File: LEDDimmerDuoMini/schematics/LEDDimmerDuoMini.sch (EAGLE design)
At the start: 13 parts, among them IC1 7805T, T1 2N3904, T2 2N3904

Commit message: Update before LED flaate testen
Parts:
- added R3, R4: (no value), eagle-ltspice:R
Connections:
- new net N$7: Q2.G, R4.2, T2.E
- net PWM1: now also R3.1, R3.2
- net PWM2: now also R4.1; no longer Q2.G, T2.E
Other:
- moved on the sheet: Q2, R2, T2
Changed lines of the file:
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@@
 <layer number="97" name="Info" color="7" fill="1" visible="yes" active="yes"/>
 <layer number="98" name="Guide" color="6" fill="1" visible="yes" active="yes"/>
+<layer number="99" name="SpiceOrder" color="5" fill="1" visible="yes" active="yes"/>
 <layer number="100" name="Muster" color="7" fill="1" visible="no" active="no"/>
 <layer number="101" name="Patch_Top" color="12" fill="4" visible="yes" active="yes"/>
@@
 <part name="R2" library="rcl" deviceset="R-EU_" device="VTA52"/>
 <part name="GND4" library="SparkFun-Aesthetics" deviceset="GND" device=""/>
+<part name="R3" library="eagle-ltspice" deviceset="R" device=""/>
+<part name="R4" library="eagle-ltspice" deviceset="R" device=""/>
 </parts>
 <sheets>
@@
 <instance part="SUPPLY1" gate="G$1" x="101.6" y="22.86"/>
 <instance part="GND3" gate="1" x="91.44" y="-38.1"/>
-<instance part="Q2" gate="G$1" x="119.38" y="7.62"/>
-<instance part="T2" gate="G1" x="111.76" y="-7.62" rot="R180"/>
-<instance part="R2" gate="G$1" x="121.92" y="-22.86" rot="R90"/>
-<instance part="GND4" gate="1" x="121.92" y="-38.1"/>
+<instance part="Q2" gate="G$1" x="132.08" y="7.62"/>
+<instance part="T2" gate="G1" x="124.46" y="-7.62" rot="R180"/>
+<instance part="R2" gate="G$1" x="134.62" y="-22.86" rot="R90"/>
+<instance part="GND4" gate="1" x="134.62" y="-38.1"/>
+<instance part="R3" gate="G$1" x="73.66" y="5.08"/>
+<instance part="R4" gate="G$1" x="116.84" y="5.08"/>
 </instances>
 <busses>
@@
 <pinref part="R2" gate="G$1" pin="1"/>
 <pinref part="GND4" gate="1" pin="GND"/>
-<wire x1="121.92" y1="-27.94" x2="121.92" y2="-30.48" width="0.1524" layer="91"/>
+<wire x1="134.62" y1="-27.94" x2="134.62" y2="-30.48" width="0.1524" layer="91"/>
 <pinref part="T2" gate="G1" pin="C"/>
-<wire x1="121.92" y1="-30.48" x2="121.92" y2="-35.56" width="0.1524" layer="91"/>
-<wire x1="109.22" y1="-12.7" x2="109.22" y2="-30.48" width="0.1524" layer="91"/>
-<wire x1="109.22" y1="-30.48" x2="121.92" y2="-30.48" width="0.1524" layer="91"/>
-<junction x="121.92" y="-30.48"/>
+<wire x1="134.62" y1="-30.48" x2="134.62" y2="-35.56" width="0.1524" layer="91"/>
+<wire x1="121.92" y1="-12.7" x2="121.92" y2="-30.48" width="0.1524" layer="91"/>
+<wire x1="121.92" y1="-30.48" x2="134.62" y2="-30.48" width="0.1524" layer="91"/>
+<junction x="134.62" y="-30.48"/>
 </segment>
 </net>
@@
 <pinref part="T1" gate="G1" pin="E"/>
 <wire x1="78.74" y1="5.08" x2="78.74" y2="-2.54" width="0.1524" layer="91"/>
-<wire x1="78.74" y1="5.08" x2="71.12" y2="5.08" width="0.1524" layer="91"/>
+<pinref part="R3" gate="G$1" pin="2"/>
 <junction x="78.74" y="5.08"/>
-<label x="71.12" y="5.08" size="1.016" layer="95" rot="R180" xref="yes"/>
+</segment>
+<segment>
+<pinref part="R3" gate="G$1" pin="1"/>
+<wire x1="68.58" y1="5.08" x2="63.5" y2="5.08" width="0.1524" layer="91"/>
+<label x="63.5" y="5.08" size="1.016" layer="95" rot="R180" xref="yes"/>
 </segment>
 </net>
@@
 <wire x1="91.44" y1="20.32" x2="91.44" y2="12.7" width="0.1524" layer="91"/>
 <pinref part="Q2" gate="G$1" pin="D"/>
-<wire x1="121.92" y1="12.7" x2="121.92" y2="20.32" width="0.1524" layer="91"/>
+<wire x1="134.62" y1="12.7" x2="121.92" y2="20.32" width="0.1524" layer="91"/>
 </segment>
 </net>
@@
 </segment>
 <segment>
-<pinref part="Q2" gate="G$1" pin="G"/>
-<wire x1="116.84" y1="5.08" x2="109.22" y2="5.08" width="0.1524" layer="91"/>
-<pinref part="T2" gate="G1" pin="E"/>
-<wire x1="109.22" y1="5.08" x2="109.22" y2="-2.54" width="0.1524" layer="91"/>
-<wire x1="109.22" y1="5.08" x2="104.14" y2="5.08" width="0.1524" layer="91"/>
-<junction x="109.22" y="5.08"/>
-<label x="104.14" y="5.08" size="1.016" layer="95" rot="R180" xref="yes"/>
+<pinref part="R4" gate="G$1" pin="1"/>
+<wire x1="111.76" y1="5.08" x2="106.68" y2="5.08" width="0.1524" layer="91"/>
+<label x="106.68" y="5.08" size="1.016" layer="95" rot="R180" xref="yes"/>
 </segment>
 </net>
@@
 <segment>
 <pinref part="T2" gate="G1" pin="B"/>
-<wire x1="121.92" y1="-7.62" x2="114.3" y2="-7.62" width="0.1524" layer="91"/>
+<wire x1="134.62" y1="-7.62" x2="127" y2="-7.62" width="0.1524" layer="91"/>
 <pinref part="R2" gate="G$1" pin="2"/>
-<wire x1="121.92" y1="-7.62" x2="121.92" y2="-17.78" width="0.1524" layer="91"/>
+<wire x1="134.62" y1="-7.62" x2="134.62" y2="-17.78" width="0.1524" layer="91"/>
 <pinref part="Q2" gate="G$1" pin="S"/>
-<wire x1="121.92" y1="2.54" x2="121.92" y2="-7.62" width="0.1524" layer="91"/>
-<junction x="121.92" y="-7.62"/>
-</segment>
-</net>
+<wire x1="134.62" y1="2.54" x2="134.62" y2="-7.62" width="0.1524" layer="91"/>
+<junction x="134.62" y="-7.62"/>
+</segment>
+</net>
+<net name="N$7" class="0">
+<segment>
+<pinref part="Q2" gate="G$1" pin="G"/>
+<pinref part="R4" gate="G$1" pin="2"/>
+<wire x1="129.54" y1="5.08" x2="121.92" y2="5.08" width="0.1524" layer="91"/>
+<pinref part="T2" gate="G1" pin="E"/>
+<wire x1="121.92" y1="-2.54" x2="121.92" y2="5.08" width="0.1524" layer="91"/>
+<junction x="121.92" y="5.08"/>
+</segment>
+</net>

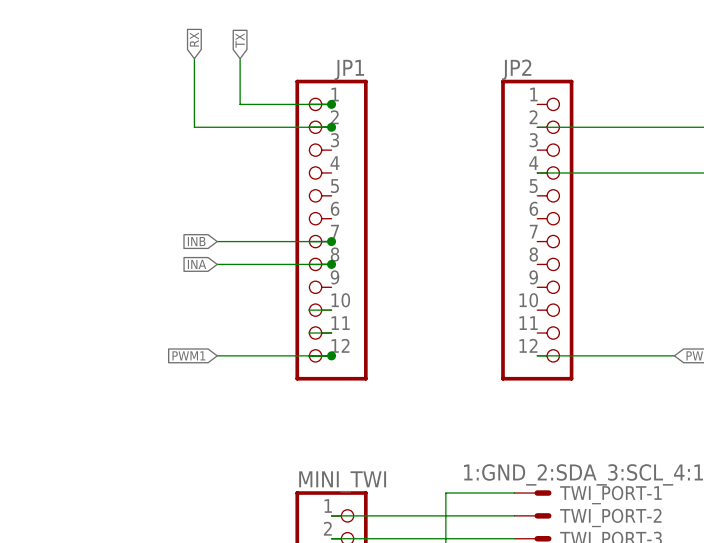
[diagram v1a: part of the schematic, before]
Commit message: Finished laying out components for LEEDDimmerDuoM<ini
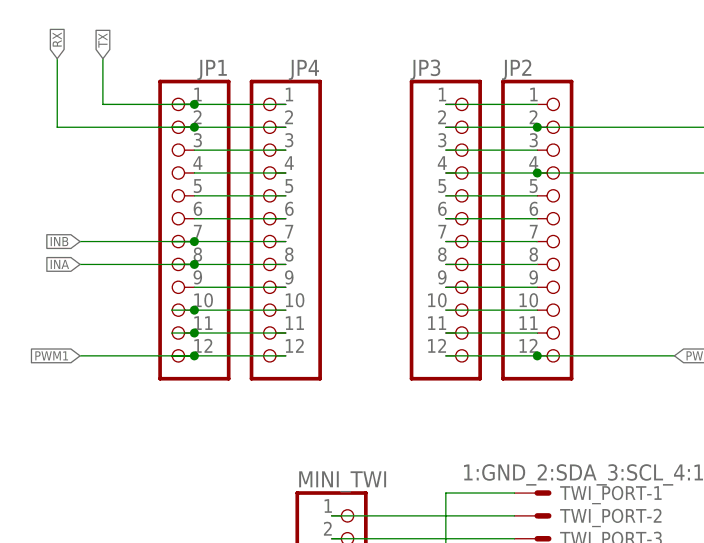
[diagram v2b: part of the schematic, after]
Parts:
- added JP3, JP4: (no value), pinhead:PINHD-1X12
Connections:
- new net N$12: JP1.6, JP4.6
- new net N$13: JP1.9, JP4.9
- new net N$15: JP2.1, JP3.1
- new net N$17: JP2.3, JP3.3
- new net N$19: JP2.5, JP3.5
- new net N$20: JP2.6, JP3.6
- new net N$21: JP2.7, JP3.7
- new net N$22: JP2.8, JP3.8
- new net N$23: JP2.9, JP3.9
- new net N$24: JP2.10, JP3.10
- new net N$25: JP2.11, JP3.11
- new net N$6: JP1.3, JP4.3
- new net N$8: JP1.4, JP4.4
- new net N$9: JP1.5, JP4.5
- net 5V: now also JP3.4
- net GND: now also JP3.2
- net INA: now also JP4.8
- net INB: now also JP4.7
- net N$10: now also JP4.11
- net N$11: now also JP4.10
- net PWM1: now also JP4.12
- net PWM2: now also JP3.12
- net RX: now also JP4.2
- net TX: now also JP4.1
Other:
- moved on the sheet: JP1
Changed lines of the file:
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@@
 <part name="R3" library="eagle-ltspice" deviceset="R" device=""/>
 <part name="R4" library="eagle-ltspice" deviceset="R" device=""/>
+<part name="JP3" library="pinhead" deviceset="PINHD-1X12" device=""/>
+<part name="JP4" library="pinhead" deviceset="PINHD-1X12" device=""/>
 </parts>
 <sheets>
@@
 <instance part="GND6" gate="1" x="121.92" y="124.46" rot="R90"/>
 <instance part="SUPPLY3" gate="G$1" x="127" y="119.38" rot="R270"/>
-<instance part="JP1" gate="G$1" x="73.66" y="114.3" rot="MR0"/>
+<instance part="JP1" gate="G$1" x="58.42" y="114.3" rot="MR0"/>
 <instance part="JP2" gate="G$1" x="101.6" y="114.3"/>
 <instance part="TWI_PORT" gate="-1" x="99.06" y="83.82" smashed="yes">
@@
 <instance part="R3" gate="G$1" x="73.66" y="5.08"/>
 <instance part="R4" gate="G$1" x="116.84" y="5.08"/>
+<instance part="JP3" gate="G$1" x="91.44" y="114.3"/>
+<instance part="JP4" gate="G$1" x="68.58" y="114.3" rot="MR0"/>
 </instances>
 <busses>
@@
 <pinref part="GND6" gate="1" pin="GND"/>
 <wire x1="99.06" y1="124.46" x2="119.38" y2="124.46" width="0.1524" layer="91"/>
+<pinref part="JP3" gate="G$1" pin="2"/>
+<wire x1="88.9" y1="124.46" x2="99.06" y2="124.46" width="0.1524" layer="91"/>
+<junction x="99.06" y="124.46"/>
 </segment>
 <segment>
@@
 <net name="INB" class="0">
 <segment>
-<wire x1="73.66" y1="111.76" x2="76.2" y2="111.76" width="0.1524" layer="91"/>
-<label x="63.5" y="111.76" size="1.016" layer="95" rot="MR0" xref="yes"/>
+<wire x1="58.42" y1="111.76" x2="60.96" y2="111.76" width="0.1524" layer="91"/>
+<label x="48.26" y="111.76" size="1.016" layer="95" rot="MR0" xref="yes"/>
 <pinref part="JP1" gate="G$1" pin="7"/>
-<wire x1="76.2" y1="111.76" x2="63.5" y2="111.76" width="0.1524" layer="91"/>
-<junction x="76.2" y="111.76"/>
+<wire x1="60.96" y1="111.76" x2="48.26" y2="111.76" width="0.1524" layer="91"/>
+<junction x="60.96" y="111.76"/>
+<pinref part="JP4" gate="G$1" pin="7"/>
+<wire x1="71.12" y1="111.76" x2="60.96" y2="111.76" width="0.1524" layer="91"/>
 </segment>
 </net>
 <net name="PWM1" class="0">
 <segment>
-<wire x1="73.66" y1="99.06" x2="76.2" y2="99.06" width="0.1524" layer="91"/>
-<label x="63.5" y="99.06" size="1.016" layer="95" rot="MR0" xref="yes"/>
+<wire x1="58.42" y1="99.06" x2="60.96" y2="99.06" width="0.1524" layer="91"/>
+<label x="48.26" y="99.06" size="1.016" layer="95" rot="MR0" xref="yes"/>
 <pinref part="JP1" gate="G$1" pin="12"/>
-<wire x1="76.2" y1="99.06" x2="63.5" y2="99.06" width="0.1524" layer="91"/>
-<junction x="76.2" y="99.06"/>
+<wire x1="60.96" y1="99.06" x2="48.26" y2="99.06" width="0.1524" layer="91"/>
+<junction x="60.96" y="99.06"/>
+<pinref part="JP4" gate="G$1" pin="12"/>
+<wire x1="71.12" y1="99.06" x2="60.96" y2="99.06" width="0.1524" layer="91"/>
 </segment>
 <segment>
@@
 <net name="INA" class="0">
 <segment>
-<wire x1="73.66" y1="109.22" x2="76.2" y2="109.22" width="0.1524" layer="91"/>
-<label x="63.5" y="109.22" size="1.016" layer="95" rot="MR0" xref="yes"/>
+<wire x1="58.42" y1="109.22" x2="60.96" y2="109.22" width="0.1524" layer="91"/>
+<label x="48.26" y="109.22" size="1.016" layer="95" rot="MR0" xref="yes"/>
 <pinref part="JP1" gate="G$1" pin="8"/>
-<wire x1="76.2" y1="109.22" x2="63.5" y2="109.22" width="0.1524" layer="91"/>
-<junction x="76.2" y="109.22"/>
+<wire x1="60.96" y1="109.22" x2="48.26" y2="109.22" width="0.1524" layer="91"/>
+<junction x="60.96" y="109.22"/>
+<pinref part="JP4" gate="G$1" pin="8"/>
+<wire x1="71.12" y1="109.22" x2="60.96" y2="109.22" width="0.1524" layer="91"/>
 </segment>
 </net>
@@
 <pinref part="JP2" gate="G$1" pin="4"/>
 <wire x1="127" y1="119.38" x2="99.06" y2="119.38" width="0.1524" layer="91"/>
+<pinref part="JP3" gate="G$1" pin="4"/>
+<wire x1="88.9" y1="119.38" x2="99.06" y2="119.38" width="0.1524" layer="91"/>
+<junction x="99.06" y="119.38"/>
 </segment>
 <segment>
@@
 <net name="RX" class="0">
 <segment>
-<wire x1="73.66" y1="124.46" x2="76.2" y2="124.46" width="0.1524" layer="91"/>
-<wire x1="76.2" y1="124.46" x2="60.96" y2="124.46" width="0.1524" layer="91"/>
-<wire x1="60.96" y1="124.46" x2="60.96" y2="132.08" width="0.1524" layer="91"/>
-<label x="60.96" y="132.08" size="1.016" layer="95" rot="R90" xref="yes"/>
+<wire x1="58.42" y1="124.46" x2="60.96" y2="124.46" width="0.1524" layer="91"/>
+<wire x1="60.96" y1="124.46" x2="45.72" y2="124.46" width="0.1524" layer="91"/>
+<wire x1="45.72" y1="124.46" x2="45.72" y2="132.08" width="0.1524" layer="91"/>
+<label x="45.72" y="132.08" size="1.016" layer="95" rot="R90" xref="yes"/>
 <pinref part="JP1" gate="G$1" pin="2"/>
-<junction x="76.2" y="124.46"/>
+<junction x="60.96" y="124.46"/>
+<pinref part="JP4" gate="G$1" pin="2"/>
+<wire x1="71.12" y1="124.46" x2="60.96" y2="124.46" width="0.1524" layer="91"/>
 </segment>
 </net>
 <net name="TX" class="0">
 <segment>
-<wire x1="73.66" y1="127" x2="76.2" y2="127" width="0.1524" layer="91"/>
-<wire x1="76.2" y1="127" x2="66.04" y2="127" width="0.1524" layer="91"/>
-<wire x1="66.04" y1="127" x2="66.04" y2="132.08" width="0.1524" layer="91"/>
-<label x="66.04" y="132.08" size="1.016" layer="95" rot="R90" xref="yes"/>
+<wire x1="58.42" y1="127" x2="60.96" y2="127" width="0.1524" layer="91"/>
+<wire x1="60.96" y1="127" x2="50.8" y2="127" width="0.1524" layer="91"/>
+<wire x1="50.8" y1="127" x2="50.8" y2="132.08" width="0.1524" layer="91"/>
+<label x="50.8" y="132.08" size="1.016" layer="95" rot="R90" xref="yes"/>
 <pinref part="JP1" gate="G$1" pin="1"/>
-<junction x="76.2" y="127"/>
+<junction x="60.96" y="127"/>
+<pinref part="JP4" gate="G$1" pin="1"/>
+<wire x1="71.12" y1="127" x2="60.96" y2="127" width="0.1524" layer="91"/>
 </segment>
 </net>
@@
 <segment>
 <pinref part="JP1" gate="G$1" pin="11"/>
-<wire x1="76.2" y1="101.6" x2="73.66" y2="101.6" width="0.1524" layer="91"/>
+<wire x1="60.96" y1="101.6" x2="58.42" y2="101.6" width="0.1524" layer="91"/>
+<pinref part="JP4" gate="G$1" pin="11"/>
+<wire x1="71.12" y1="101.6" x2="60.96" y2="101.6" width="0.1524" layer="91"/>
+<junction x="60.96" y="101.6"/>
 </segment>
 </net>
@@
 <segment>
 <pinref part="JP1" gate="G$1" pin="10"/>
-<wire x1="76.2" y1="104.14" x2="73.66" y2="104.14" width="0.1524" layer="91"/>
+<wire x1="60.96" y1="104.14" x2="58.42" y2="104.14" width="0.1524" layer="91"/>
+<pinref part="JP4" gate="G$1" pin="10"/>
+<wire x1="71.12" y1="104.14" x2="60.96" y2="104.14" width="0.1524" layer="91"/>
+<junction x="60.96" y="104.14"/>
 </segment>
 </net>
@@
 <wire x1="99.06" y1="99.06" x2="114.3" y2="99.06" width="0.1524" layer="91"/>
 <label x="114.3" y="99.06" size="1.016" layer="95" xref="yes"/>
+<pinref part="JP3" gate="G$1" pin="12"/>
+<wire x1="88.9" y1="99.06" x2="99.06" y2="99.06" width="0.1524" layer="91"/>
+<junction x="99.06" y="99.06"/>
 </segment>
 <segment>
@@
 </segment>
 </net>
+<net name="N$6" class="0">
+<segment>
+<pinref part="JP4" gate="G$1" pin="3"/>
+<pinref part="JP1" gate="G$1" pin="3"/>
+<wire x1="71.12" y1="121.92" x2="60.96" y2="121.92" width="0.1524" layer="91"/>
+</segment>
+</net>
+<net name="N$8" class="0">
+<segment>
+<pinref part="JP4" gate="G$1" pin="4"/>
+<pinref part="JP1" gate="G$1" pin="4"/>
+<wire x1="71.12" y1="119.38" x2="60.96" y2="119.38" width="0.1524" layer="91"/>
+</segment>
+</net>
+<net name="N$9" class="0">
+<segment>
+<pinref part="JP4" gate="G$1" pin="5"/>
+<pinref part="JP1" gate="G$1" pin="5"/>
+<wire x1="71.12" y1="116.84" x2="60.96" y2="116.84" width="0.1524" layer="91"/>
+</segment>
+</net>
+<net name="N$12" class="0">
+<segment>
+<pinref part="JP4" gate="G$1" pin="6"/>
+<pinref part="JP1" gate="G$1" pin="6"/>
+<wire x1="71.12" y1="114.3" x2="60.96" y2="114.3" width="0.1524" layer="91"/>
+</segment>
+</net>
+<net name="N$13" class="0">
+<segment>
+<pinref part="JP4" gate="G$1" pin="9"/>
+<pinref part="JP1" gate="G$1" pin="9"/>
+<wire x1="71.12" y1="106.68" x2="60.96" y2="106.68" width="0.1524" layer="91"/>
+</segment>
+</net>
+<net name="N$15" class="0">
+<segment>
+<pinref part="JP3" gate="G$1" pin="1"/>
+<pinref part="JP2" gate="G$1" pin="1"/>
+<wire x1="88.9" y1="127" x2="99.06" y2="127" width="0.1524" layer="91"/>
+</segment>
+</net>
+<net name="N$17" class="0">
+<segment>
+<pinref part="JP2" gate="G$1" pin="3"/>
+<pinref part="JP3" gate="G$1" pin="3"/>
+<wire x1="99.06" y1="121.92" x2="88.9" y2="121.92" width="0.1524" layer="91"/>
+</segment>
+</net>
+<net name="N$19" class="0">
+<segment>
+<pinref part="JP3" gate="G$1" pin="5"/>
+<pinref part="JP2" gate="G$1" pin="5"/>
+<wire x1="88.9" y1="116.84" x2="99.06" y2="116.84" width="0.1524" layer="91"/>
+</segment>
+</net>
+<net name="N$20" class="0">
+<segment>
+<pinref part="JP3" gate="G$1" pin="6"/>
+<pinref part="JP2" gate="G$1" pin="6"/>
+<wire x1="88.9" y1="114.3" x2="99.06" y2="114.3" width="0.1524" layer="91"/>
+</segment>
+</net>
+<net name="N$21" class="0">
+<segment>
+<pinref part="JP3" gate="G$1" pin="7"/>
+<pinref part="JP2" gate="G$1" pin="7"/>
+<wire x1="88.9" y1="111.76" x2="99.06" y2="111.76" width="0.1524" layer="91"/>
+</segment>
+</net>
+<net name="N$22" class="0">
+<segment>
+<pinref part="JP3" gate="G$1" pin="8"/>
+<pinref part="JP2" gate="G$1" pin="8"/>
+<wire x1="88.9" y1="109.22" x2="99.06" y2="109.22" width="0.1524" layer="91"/>
+</segment>
+</net>
+<net name="N$23" class="0">
+<segment>
+<pinref part="JP3" gate="G$1" pin="9"/>
+<pinref part="JP2" gate="G$1" pin="9"/>
+<wire x1="88.9" y1="106.68" x2="99.06" y2="106.68" width="0.1524" layer="91"/>
+</segment>
+</net>
+<net name="N$24" class="0">
+<segment>
+<pinref part="JP3" gate="G$1" pin="10"/>
+<pinref part="JP2" gate="G$1" pin="10"/>
+<wire x1="88.9" y1="104.14" x2="99.06" y2="104.14" width="0.1524" layer="91"/>
+</segment>
+</net>
+<net name="N$25" class="0">
+<segment>
+<pinref part="JP3" gate="G$1" pin="11"/>
+<pinref part="JP2" gate="G$1" pin="11"/>
+<wire x1="88.9" y1="101.6" x2="99.06" y2="101.6" width="0.1524" layer="91"/>
+</segment>
+</net>
